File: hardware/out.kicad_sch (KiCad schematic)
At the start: 1 part, among them J201 Screw_Terminal_01x04

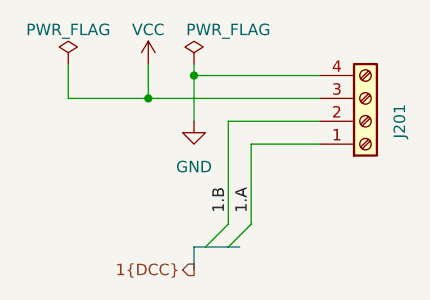
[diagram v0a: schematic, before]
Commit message: changed LDO
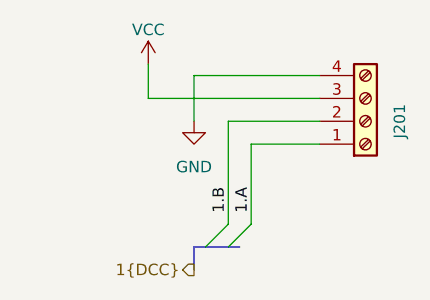
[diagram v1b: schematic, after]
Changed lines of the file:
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@@
 	(generator_version "8.0")
 	(paper "A4")
-	(junction
-		(at 162.56 106.68)
-		(diameter 0)
-		(color 0 0 0 0)
-	)
-	(junction
-		(at 167.64 104.14)
-		(diameter 0)
-		(color 0 0 0 0)
-	)
 	(bus_entry
 		(at 171.45 123.19)
@@
 		)
 	)
-	(wire
-		(pts
-			(xy 153.67 106.68) (xy 153.67 102.87)
-		)
-		(stroke
-			(width 0)
-			(type default)
-		)
-	)
 	(bus
 		(pts
@@
 	(wire
 		(pts
-			(xy 162.56 106.68) (xy 153.67 106.68)
-		)
-		(stroke
-			(width 0)
-			(type default)
-		)
-	)
-	(wire
-		(pts
 			(xy 181.61 109.22) (xy 171.45 109.22)
 		)
@@
 		(pts
 			(xy 181.61 106.68) (xy 162.56 106.68)
-		)
-		(stroke
-			(width 0)
-			(type default)
-		)
-	)
-	(wire
-		(pts
-			(xy 167.64 102.87) (xy 167.64 104.14)
 		)
 		(stroke
@@
 				(path "/5298ac75-044e-4260-bbaf-3f2b608479b0/05187f9e-02b7-4d4f-ab81-0ead3ebc451f"
 					(reference "J201")
-					(unit 1)
-				)
-			)
-		)
-	)
-	(symbol
-		(lib_id "power:PWR_FLAG")
-		(at 153.67 102.87 0)
-		(mirror y)
-		(unit 1)
-		(exclude_from_sim no)
-		(in_bom yes)
-		(on_board yes)
-		(dnp no)
-		(property "Reference" "#FLG0202"
-			(at 153.67 100.965 0)
-			(effects
-				(font
-					(size 1.27 1.27)
-				)
-				(hide yes)
-			)
-		)
-		(property "Value" "PWR_FLAG"
-			(at 153.67 99.06 0)
-			(effects
-				(font
-					(size 1.27 1.27)
-				)
-			)
-		)
-		(property "Footprint" ""
-			(at 153.67 102.87 0)
-			(effects
-				(font
-					(size 1.27 1.27)
-				)
-				(hide yes)
-			)
-		)
-		(property "Datasheet" "~"
-			(at 153.67 102.87 0)
-			(effects
-				(font
-					(size 1.27 1.27)
-				)
-				(hide yes)
-			)
-		)
-		(property "Description" ""
-			(at 153.67 102.87 0)
-			(effects
-				(font
-					(size 1.27 1.27)
-				)
-				(hide yes)
-			)
-		)
-		(pin "1"
-		)
-		(instances
-			(project "oneFit"
-				(path "/5298ac75-044e-4260-bbaf-3f2b608479b0/05187f9e-02b7-4d4f-ab81-0ead3ebc451f"
-					(reference "#FLG0202")
 					(unit 1)
 				)
@@
 					(unit 1)
 				)
-			)
-		)
-	)
-	(symbol
-		(lib_id "power:PWR_FLAG")
-		(at 167.64 102.87 0)
-		(mirror y)
-		(unit 1)
-		(exclude_from_sim no)
-		(in_bom yes)
-		(on_board yes)
-		(dnp no)
-		(property "Reference" "#FLG0201"
-			(at 167.64 100.965 0)
-			(effects
-				(font
-					(size 1.27 1.27)
-				)
-				(hide yes)
-			)
-		)
-		(property "Value" "PWR_FLAG"
-			(at 171.45 99.06 0)
-			(effects
-				(font
-					(size 1.27 1.27)
-				)
-			)
-		)
-		(property "Footprint" ""
-			(at 167.64 102.87 0)
-			(effects
-				(font
-					(size 1.27 1.27)
-				)
-				(hide yes)
-			)
-		)
-		(property "Datasheet" "~"
-			(at 167.64 102.87 0)
-			(effects
-				(font
-					(size 1.27 1.27)
-				)
-				(hide yes)
-			)
-		)
-		(property "Description" ""
-			(at 167.64 102.87 0)
-			(effects
-				(font
-					(size 1.27 1.27)
-				)
-				(hide yes)
-			)
-		)
-		(pin "1"
-		)
-		(instances
-			(project "oneFit"
-				(path "/5298ac75-044e-4260-bbaf-3f2b608479b0/05187f9e-02b7-4d4f-ab81-0ead3ebc451f"
-					(reference "#FLG0201")
-					(unit 1)
-				)

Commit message: upadted readme
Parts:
- J201: JLCPCB Part# C880574 -> C6394075
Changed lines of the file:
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@@
 			)
 		)
-		(property "JLCPCB Part#" "C880574"
+		(property "JLCPCB Part#" "C6394075"
 			(at 186.69 109.22 0)
 			(effects
